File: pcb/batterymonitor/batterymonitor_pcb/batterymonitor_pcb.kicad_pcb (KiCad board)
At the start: 2 copper layers, 65 x 45 mm, 8 parts, among them J1 12V_Input, U1 AMS1117-3.3

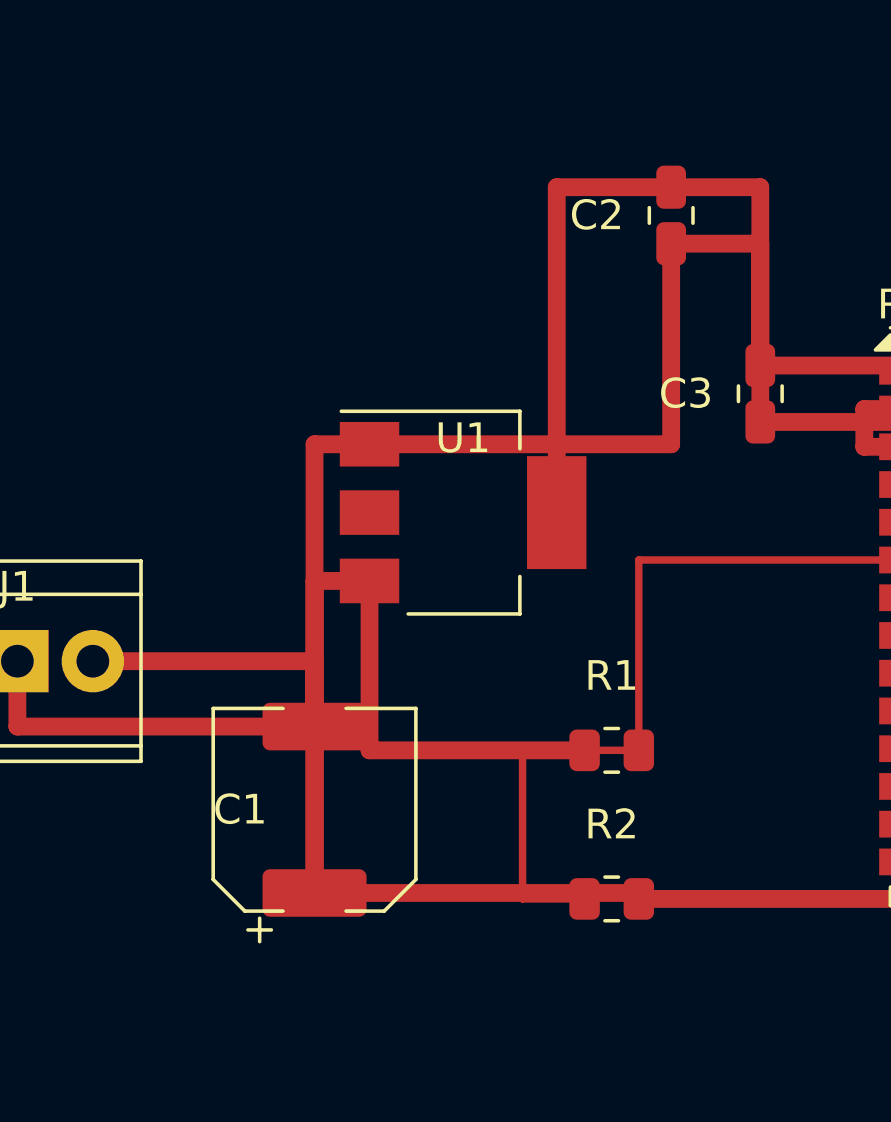
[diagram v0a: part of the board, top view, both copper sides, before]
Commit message: Implement AP63300 buck converter design in PCB and schematic
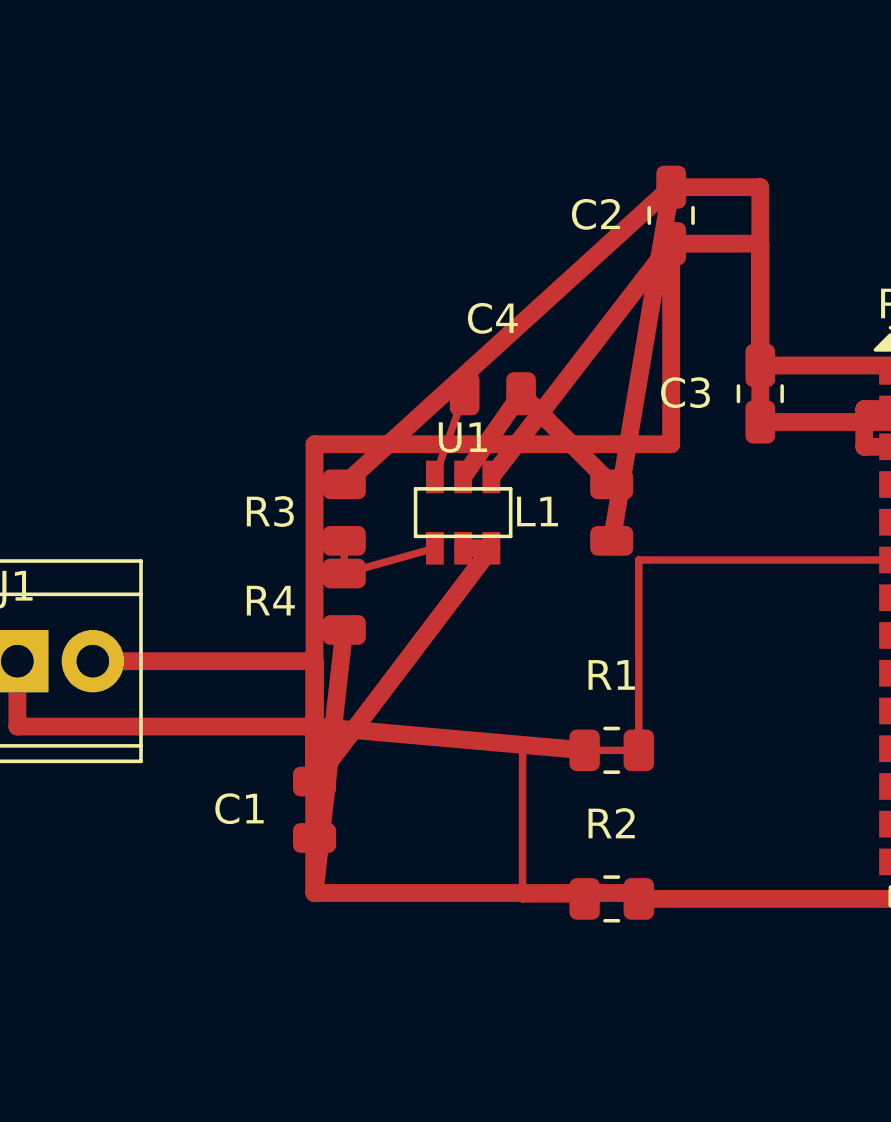
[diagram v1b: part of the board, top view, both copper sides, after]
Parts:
- added C4: 100nF/50V, Capacitor_SMD:C_0805_2012Metric, F.Cu at (106.0, 66.0)
- added L1: 4.7uH, Inductor_SMD:L_0806_2012Metric, F.Cu at (110.0, 70.0)
- added R3: 100k, Resistor_SMD:R_0805_2012Metric, F.Cu at (101.0, 70.0)
- added R4: 32k, Resistor_SMD:R_0805_2012Metric, F.Cu at (101.0, 73.0)
- C1: value 100uF/25V -> 10uF/25V; footprint Capacitor_SMD:CP_Elec_6.3x5.4 -> Capacitor_SMD:C_0805_2012Metric
- C2: value 10uF/6.3V -> 22uF/10V
- U1: value AMS1117-3.3 -> AP63300; footprint Package_TO_SOT_SMD:SOT-223-3_TabPin2 -> Package_TO_SOT_SMD:TSOT-23-6
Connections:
- U1 pad 1: GND -> FB
- U1 pad 2: 3.3V -> 12V
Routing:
- net GND: track 87.7 -> 106.5 mm
- net 3.3V: track 33.8 -> 45.9 mm
- net SW: track 0.00 -> 7.73 mm
- net FB: track 0.00 -> 4.27 mm
- net BST: track 0.00 -> 2.97 mm
- net 12V: track 31.9 -> 34.0 mm

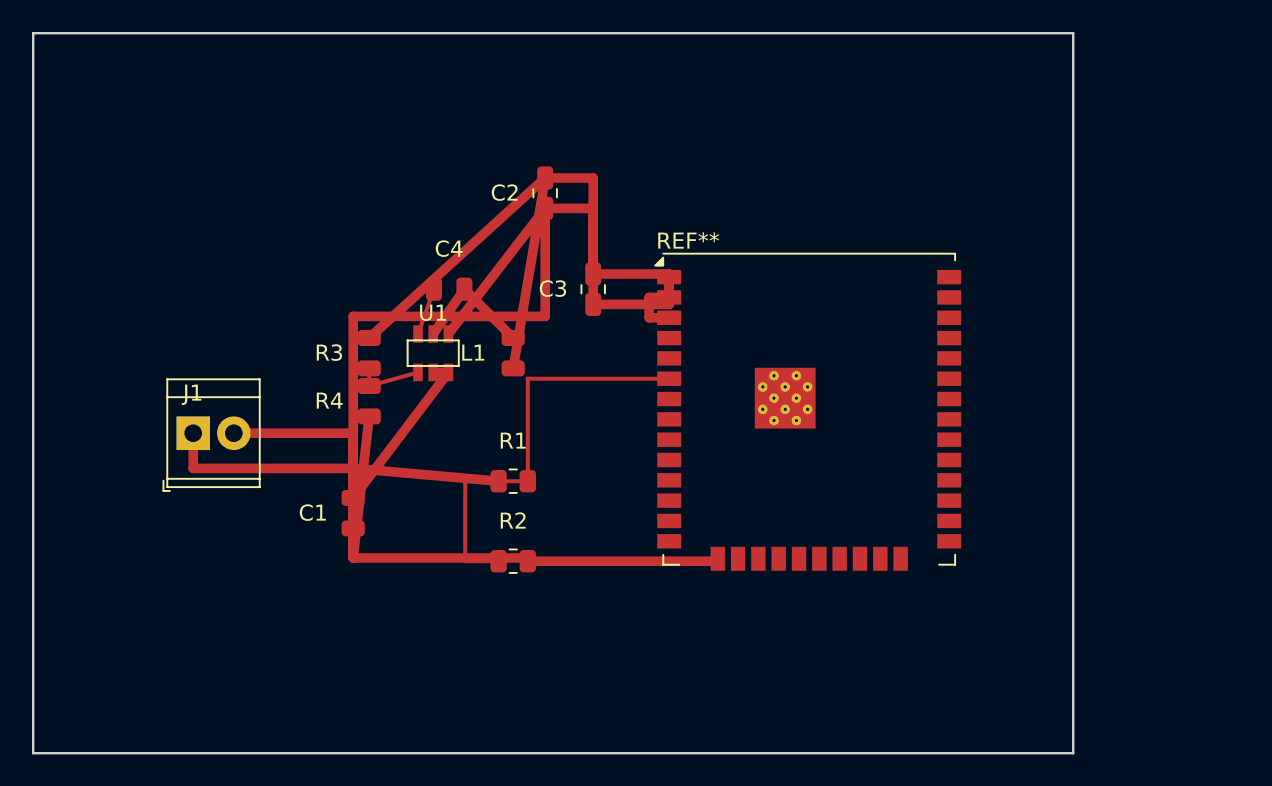
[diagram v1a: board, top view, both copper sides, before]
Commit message: Add DC Jack Female component to BOM files for battery monitor PCB
- Added DC Jack Female (J4) to both bom_jlcpcb.csv and bom_pcbway.csv
- Updated component details including footprint and manufacturer information
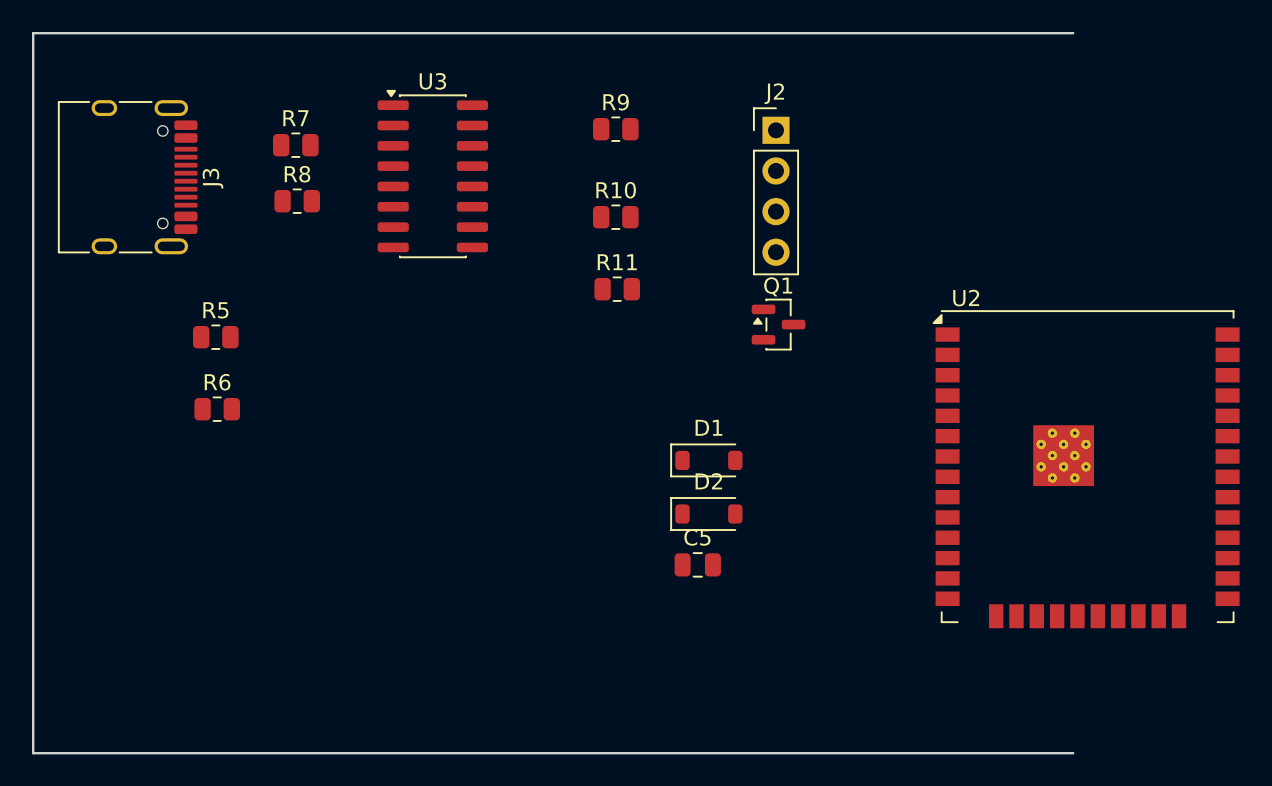
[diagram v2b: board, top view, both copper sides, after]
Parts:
- removed C1: 10uF/25V, Capacitor_SMD:C_0805_2012Metric
- removed C2: 22uF/10V, Capacitor_SMD:C_0805_2012Metric
- removed C3: 100nF/10V, Capacitor_SMD:C_0805_2012Metric
- removed C4: 100nF/50V, Capacitor_SMD:C_0805_2012Metric
- removed J1: 12V_Input, TerminalBlock_TE-Connectivity:TerminalBlock_TE_282834-2_1x02_P2.54mm_Horizontal
- removed L1: 4.7uH, Inductor_SMD:L_0806_2012Metric
- removed R1, R3: 100k, Resistor_SMD:R_0805_2012Metric
- removed R2: 22k, Resistor_SMD:R_0805_2012Metric
- removed R4: 32k, Resistor_SMD:R_0805_2012Metric
- removed REF**: ESP32-WROOM-32U, RF_Module:ESP32-WROOM-32U
- removed U1: AP63300, Package_TO_SOT_SMD:TSOT-23-6
- added C5: 100nF/10V, Capacitor_SMD:C_0805_2012Metric, F.Cu at (121.5, 83.2)
- added D1: SS14, Diode_SMD:D_SOD-123, F.Cu at (122.2, 76.7)
- added D2: SS14, Diode_SMD:D_SOD-123, F.Cu at (122.2, 80.0)
- added J2: Conn_01x04_Pin, Connector_PinHeader_2.54mm:PinHeader_1x04_P2.54mm_Vertical, F.Cu at (126.4, 56.1)
- added J3: USB_C_Receptacle_HRO_TYPE-C-31-M-12, Connector_USB:USB_C_Receptacle_HRO_TYPE-C-31-M-12, F.Cu at (85.5, 59.0)
- added Q1: S8050, Package_TO_SOT_SMD:SOT-23, F.Cu at (126.6, 68.2)
- added R10: 10k, Resistor_SMD:R_0805_2012Metric, F.Cu at (116.4, 61.5)
- added R11: 10k, Resistor_SMD:R_0805_2012Metric, F.Cu at (116.5, 66.0)
- added R5: 1k, Resistor_SMD:R_0805_2012Metric, F.Cu at (91.4, 69.0)
- added R6: 1k, Resistor_SMD:R_0805_2012Metric, F.Cu at (91.5, 73.5)
- added R7: 5.1k, Resistor_SMD:R_0805_2012Metric, F.Cu at (96.4, 57.0)
- added R8: 5.1k, Resistor_SMD:R_0805_2012Metric, F.Cu at (96.5, 60.5)
- added R9: 10k, Resistor_SMD:R_0805_2012Metric, F.Cu at (116.4, 56.0)
- added U2: ESP32-WROOM-32U-N4, RF_Module:ESP32-WROOM-32U, F.Cu at (145.9, 77.1)
- added U3: CH340C, Package_SO:SOIC-16_3.9x9.9mm_P1.27mm, F.Cu at (105.0, 58.9)
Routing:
- net GND: track 106.5 -> 0.00 mm
- net 3.3V: track 45.9 -> 0.00 mm
- net 12V: track 34.0 -> 0.00 mm
- net V_ADC: track 26.2 -> 0.00 mm
- net SW: track 7.73 -> 0.00 mm
- net FB: track 4.27 -> 0.00 mm
- net BST: track 2.97 -> 0.00 mm
